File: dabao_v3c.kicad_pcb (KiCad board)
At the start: 6 copper layers, 17.8 x 21.1 mm, 69 parts, among them J1 USB_C_Receptacle_USB2.0_16P, Q1 LP0404N3T5G, Q2 LN237N3T5G, SW1 SKTAAAE010, SW2 SKTAAAE010, U1 baochip1x, U3 SMD IC PMIC;DCDC Buck-ADJ-1A,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, U4 XIAO-HALF-HOLE-23P, U5 EMS4000RSW, U7 SGM40567-4.2XG/TR, U8 SX1801CCR, U9 SMD IC PMIC;DCDC Buck-ADJ-1A,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, Y2 48.000MHz

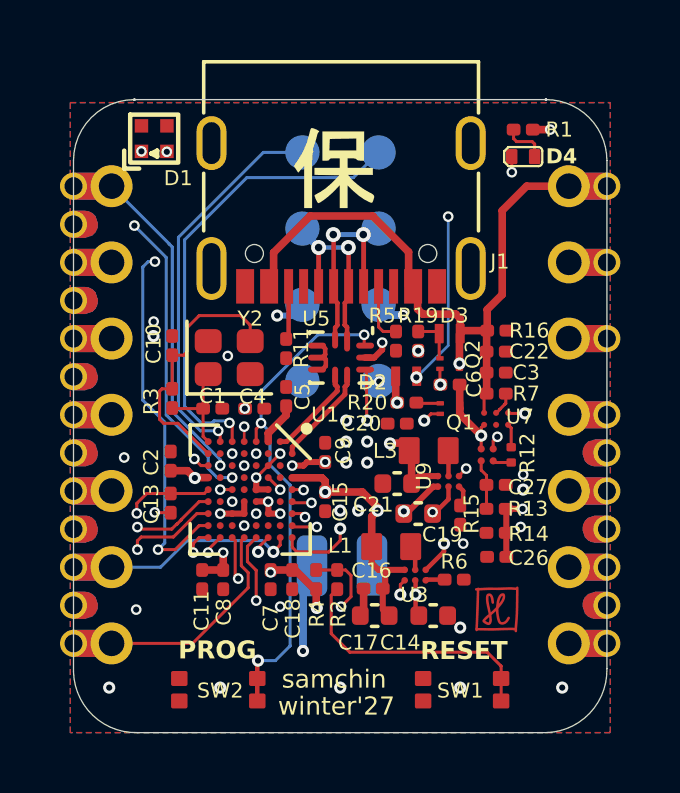
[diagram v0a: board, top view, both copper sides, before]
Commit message: with pc0-pc9 and pb11-pb14
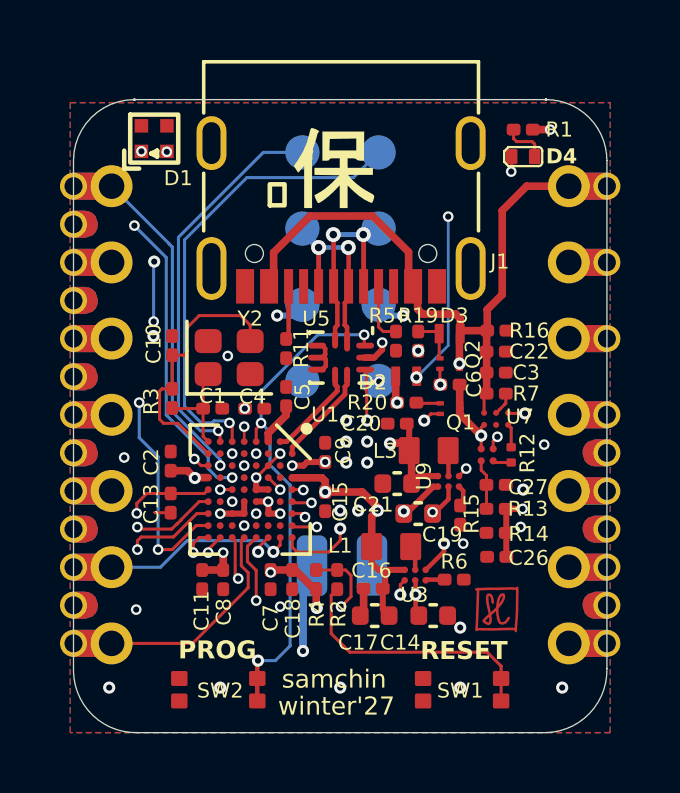
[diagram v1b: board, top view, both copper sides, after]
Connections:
- D1 pad 3: /PC3/WS2812B_LED -> /PA1/WS2812B_LED
- D4 pad -: /PC4/LED -> /PB2/LED
- U1 pad A8: /PB2 -> /PB2/LED
- U1 pad E8: /PC4/LED -> /PC4
- U1 pad F2: /PA1 -> /PA1/WS2812B_LED
- U1 pad H8: /PC3/WS2812B_LED -> /PC3
- U4 pad 17: /PA1 -> /PC3
- U4 pad 23: /PB2 -> /PC4
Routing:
- net /PC4/LED: track 23.8 -> 0.00 mm, vias 2 -> 0
- net /PB2/LED: track 0.00 -> 19.0 mm, vias 0 -> 2
- net /PC3/WS2812B_LED: track 16.2 -> 0.00 mm, vias 3 -> 0
- net /PC4: track 0.00 -> 15.7 mm, vias 0 -> 2
- net /PA1/WS2812B_LED: track 0.00 -> 12.0 mm, vias 0 -> 4
- net /PB2: track 11.5 -> 0.00 mm, vias 2 -> 0
- net /PC3: track 0.00 -> 9.94 mm, vias 0 -> 2
- net /PA1: track 9.64 -> 0.00 mm, vias 2 -> 0
- net /PB5: track 10.2 -> 9.04 mm
- net /PB13: track 14.4 -> 15.5 mm
- net +3.3V: track 12.4 -> 13.4 mm
- net /PB3: track 6.57 -> 7.21 mm
- net GND: vias 30 -> 29
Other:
- board text added: "xiao bao v1"
- board text added: "小"
- board text removed: "xiao bao (小保) v1"

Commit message: fixed the fact that pa0 was a lie
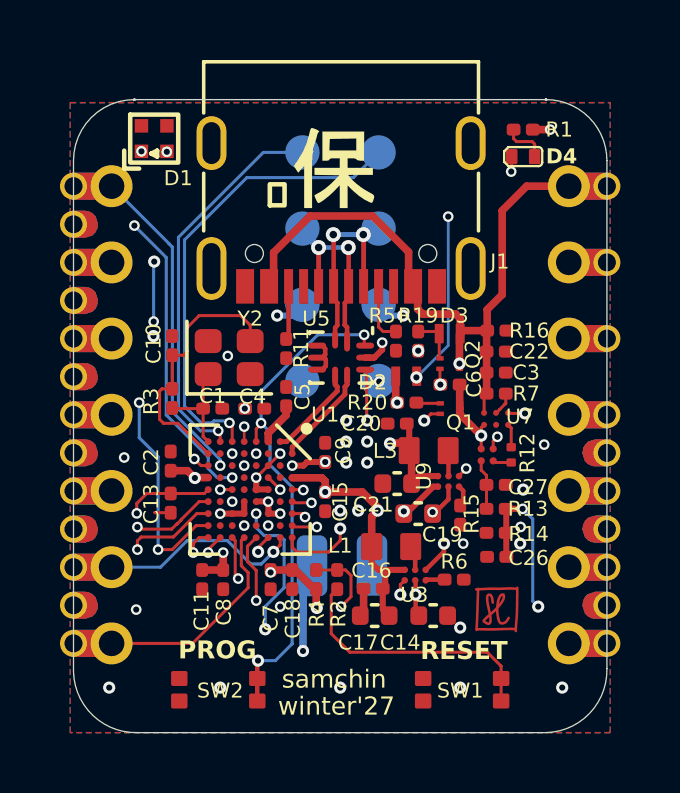
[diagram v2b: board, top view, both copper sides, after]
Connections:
- U1 pad C8: unconnected-(U1C-PB9-PadC8) -> /PB9
- U4 pad 21: /PA0 -> /PB9
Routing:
- net /PB9: track 0.00 -> 13.2 mm, vias 0 -> 2
- net /PA7/ADC3: track 13.3 -> 20.6 mm, vias 2 -> 4
